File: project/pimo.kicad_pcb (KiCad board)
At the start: 2 copper layers, 65 x 56.5 mm, 8 parts, among them J1 RPi_GPIO, J11 Conn_01x03_Pin, U1 W25Q32JVSS

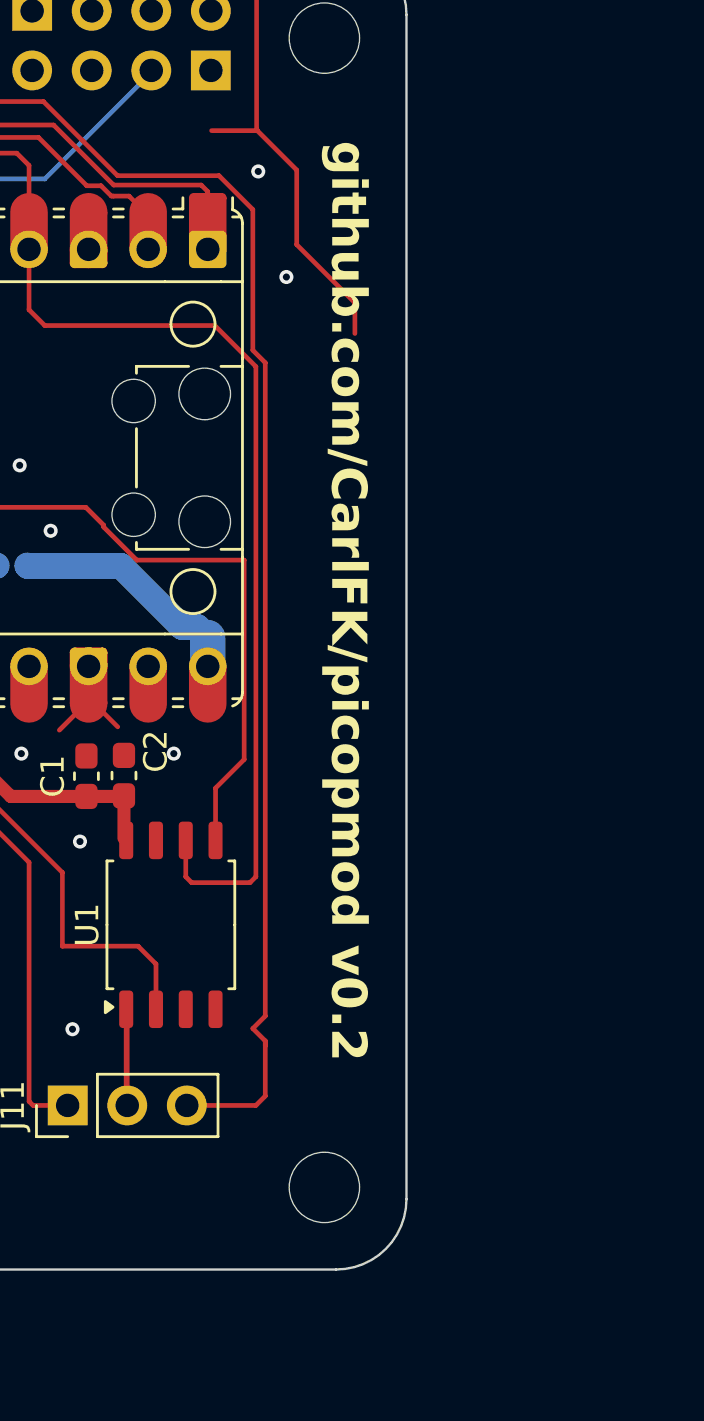
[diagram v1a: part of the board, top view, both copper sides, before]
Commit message: jtag symbol added
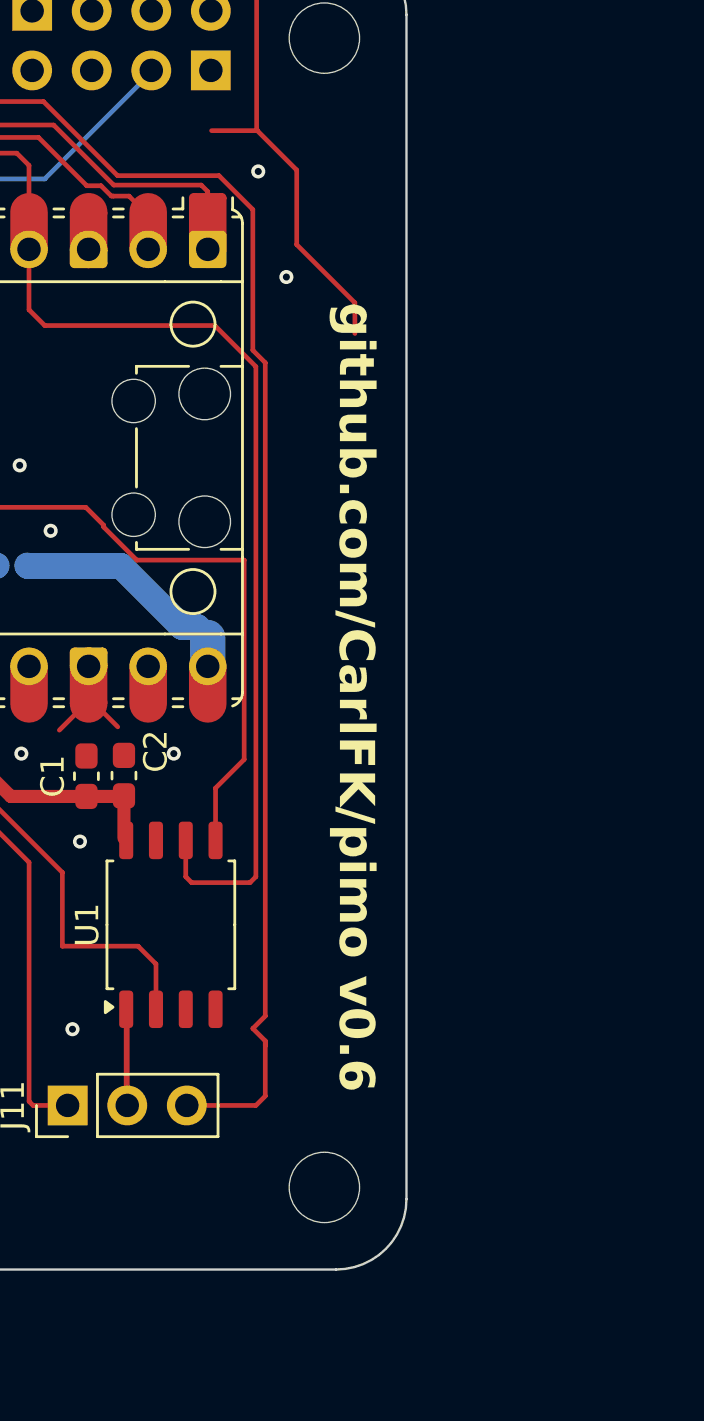
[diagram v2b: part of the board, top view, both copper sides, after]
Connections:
- net /TCK renamed /SWCLK/TCK
- net /TDI renamed /NC/TDI
- net /TDO renamed /SWO/TDO
- net /TMS renamed /SWDIO/TMS
- net /TRST renamed /RESET
- A1 pad 21: unconnected-(A1-GPIO16-Pad21) -> Net-(A1-GPIO16)
- A1 pad 22: unconnected-(A1-GPIO17-Pad22) -> Net-(A1-GPIO17)
- A1 pad 24: unconnected-(A1-GPIO18-Pad24) -> Net-(A1-GPIO18)
- A1 pad 25: unconnected-(A1-GPIO19-Pad25) -> Net-(A1-GPIO19)
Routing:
- net unconnected-(A1-GPIO19-Pad25): track 142.1 -> 0.00 mm
- net Net-(A1-GPIO19): track 0.00 -> 142.1 mm
- net unconnected-(J1-BCM27-Pad13): track 0.00 -> 42.5 mm
- net /SWDIO/TMS: track 42.5 -> 0.00 mm
- net unconnected-(J1-BCM26-Pad37): track 0.00 -> 25.2 mm
- net /NC/TDI: track 25.2 -> 0.00 mm
- net unconnected-(J1-BCM25-Pad22): track 0.00 -> 11.5 mm
- net /SWCLK/TCK: track 11.5 -> 0.00 mm
- net unconnected-(J1-BCM24-Pad18): track 0.00 -> 11.3 mm
- net /SWO/TDO: track 11.3 -> 0.00 mm
- net unconnected-(J1-BCM22-Pad15): track 0.00 -> 10.9 mm
- net /RESET: track 10.9 -> 0.00 mm
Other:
- board text added: "github.com/CarlFK/pimo v0.6"
- board text removed: "github.com/CarlFK/picopmod v0.2"
